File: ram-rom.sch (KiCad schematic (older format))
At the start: 0 parts

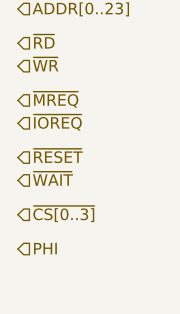
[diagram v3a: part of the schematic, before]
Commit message: toplevel: Add in SPI_SSx, IRQx, and INSTRD
  - Create the SPI_SSx and IRQx pins in the CPU schematic
  - Create the INSTRD pin in the memory schematic
  - Wire things up on the toplevel
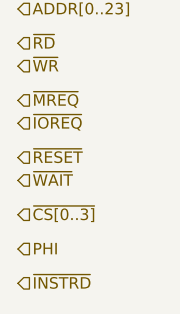
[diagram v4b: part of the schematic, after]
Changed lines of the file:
@@
 $Descr A4 11693 8268
 encoding utf-8
-Sheet 7 8
+Sheet 8 8
 Title ""
 Date ""
@@
 Text HLabel 9800 2700 2    50   Input ~ 0
 PHI
+Text HLabel 9800 2850 2    50   Input ~ 0
+~INSTRD
 $EndSCHEMATC

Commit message: memory: Add in three 32Mb SRAM chips
This is the initial version of the 32Mb SRAM symbols and initial
placement in the memory subsheet. Things to do still:

  - Import the the PLA chip symbol and wire it up
  - Import the EEPROM Boot ROM chip symbol and wire it up
  - Wire in power and decoupling chips
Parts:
- added U? (x3): IS61-64WV204816BLL, symbol Zippy:IS61-64WV204816BLL
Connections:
- net labels added: ADDR0, ADDR1, ADDR10, ADDR11, ADDR12, ADDR13, ADDR14, ADDR15, ADDR16, ADDR17, ADDR18, ADDR19, ADDR2, ADDR20, ADDR3, ADDR4, ADDR5, ADDR6, ADDR7, ADDR8, ADDR9, DATA0, DATA1, DATA10, DATA11, DATA12, DATA13, DATA14, DATA15, DATA2, DATA3, DATA4, DATA5, DATA6, DATA7, DATA8, DATA9
- wire segments 0 -> 117

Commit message: Major rework of the system RAM integration   - Wired up the jellybean logic for the RAM chip selects.   - Reorganized various bits here and there.   - Added preliminary symbols for the jellybean logic.
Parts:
- added C?: 0.1uF, symbol Device:C_Small
- added U? (x3): SN74ALVC10, symbol Zippy:SN74ALVC10
- added U?: SN74ALVC04, symbol Zippy:SN74ALVC04
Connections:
- net labels added: +3V3, ADDR21, ADDR22, ADDR23, CS1, GND, SRAM0_LB, SRAM0_UB, SRAM1_LB, SRAM1_UB, SRAM2_LB, SRAM2_UB, ~ADDR21, ~ADDR22, ~ADDR23, ~ADDR[20..23], ~SRAM0_CS, ~SRAM1_CS, ~SRAM2_CS
- net labels removed: PHI, ~CS[0..3], ~INSTRD, ~IOREQ, ~MREQ, ~RESET, ~WAIT
- wire segments 117 -> 158
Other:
- note added: "SRAM Decoded Chip Select and Address Outputs"

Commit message: boot rom: Add in the symbol for the Flash and integrate into the system   - Add the Flash ROM schematic symbol.   - Add to the ram-rom schematic.   - Get rid of /INSTRD -- not really useful.   - Export /CS0 so we can select the Flash ROM.
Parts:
- added C? (x4): 10nF, symbol Device:C_Small
- added RN?: 0 Ohm, symbol Device:R_Pack08
- added U?: SST39LF040-55-4C-NHE, symbol Zippy:SST39LF040-55-4C-NHE
- added U? (x3): IS61-64WV204816BLL, symbol Zippy:IS61-64WV204816BLL
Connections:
- net labels added: UB_DATA0, UB_DATA1, UB_DATA2, UB_DATA3, UB_DATA4, UB_DATA5, UB_DATA6, UB_DATA7, ~CS0
- net labels removed: DATA10, DATA11, DATA12, DATA13, DATA14, DATA15, DATA8, DATA9
- wire segments 158 -> 247
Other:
- note added: "Boot Flash ROM"
- note added: "SRAM Chips"
- note added: "SRAM Power and Decoupling"
- note added: "SRAM Upper Byte Data Line Safety"
